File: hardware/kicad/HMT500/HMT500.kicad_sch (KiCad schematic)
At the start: 0 parts

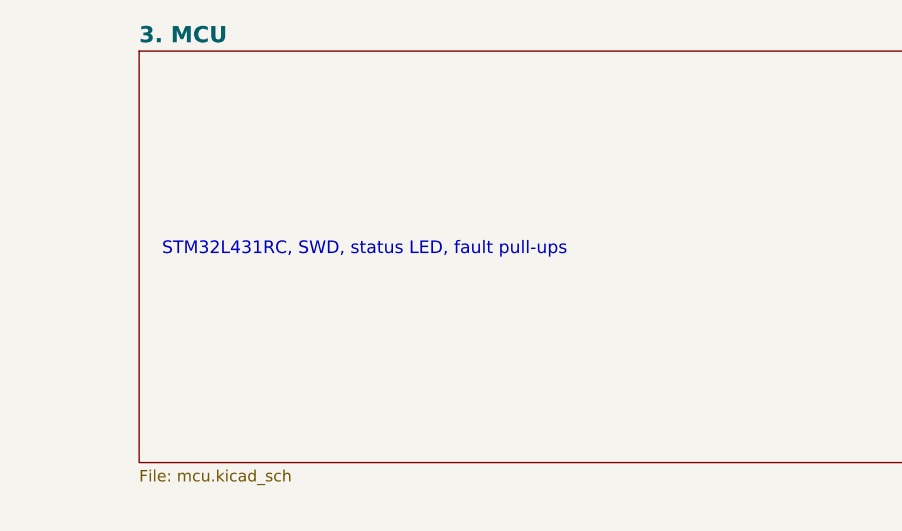
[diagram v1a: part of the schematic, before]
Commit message: Switch MCU to STM32G0B1CCT3 (in-house part, 125 C grade)
DOTECH already uses the STM32G0B1CCT6 in DP2000. Use the -40..125 C
grade of the same chip so tooling, drivers and production fixtures
can be shared.

- Schematic: new LQFP48 symbol with pin numbers from the official
  KiCad STM32G0B1C_B-C-E_Tx symbol. NRST is on PF2. BOOT0 shares
  PA14/SWCLK, so the pull-down is removed and the option bytes select
  flash boot. SWO is gone (Cortex-M0+), so J2 pin 6 is NC. VREF+ is
  fed from the FB2 filter. Faults and alarms move to PB13-15. The
  netlist check passes: 69 nets, 0 errors.
- Pin table, block design, BOM and cost updated. The bootloader doc
  now covers G0B1 dual-bank page erase, the prefetch erratum and the
  option bytes.
- Mech: MCU footprint in the 3D and drawings is now 7x7. STEP files,
  renders and the KiCad board regenerated.
- MCU review: fix product names read from the purchase report
  (HPX3000, HTP1100W) and mark the decision.

Co-Authored-By: Claude Opus 5.5 <noreply@anthropic.com>
Claude-Session: https://claude.ai/code/session_01JA2o8uJsqp9Vzsg4b665ev
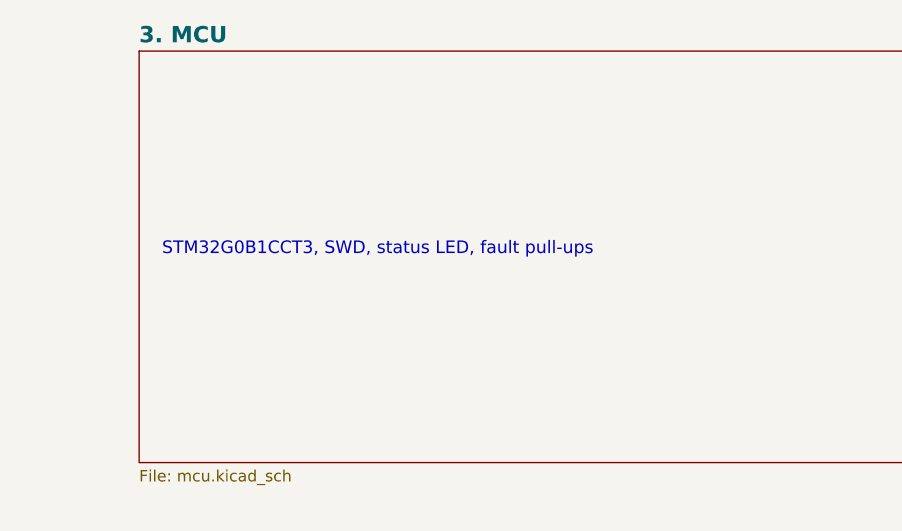
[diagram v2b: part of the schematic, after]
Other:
- note added: "STM32G0B1CCT3, SWD, status LED, fault pull-ups"
- note removed: "STM32L431RC, SWD, status LED, fault pull-ups"
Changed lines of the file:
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@@
 (text "eFuse (reverse/OV/UV), 60V buck to 5V, LDO 3.3V" (at 160.02 78.74 0) (effects (font (size 1.4 1.4)) (justify left bottom)))
 (sheet (at 284.48 55.88) (size 106.68 45.72) (fields_autoplaced) (stroke (width 0.1524) (type solid)) (fill (color 0 0 0 0.0000)) (property "Sheetname" "3. MCU" (at 284.48 55.118 0) (effects (font (size 1.8 1.8) bold) (justify left bottom))) (property "Sheetfile" "mcu.kicad_sch" (at 284.48 102.362 0) (effects (font (size 1.27 1.27)) (justify left top))) (instances (project "HMT500" (path "/1ebb025b-11bd-5f7c-aaab-41e2a750e8b3" (page "4")))))
-(text "STM32L431RC, SWD, status LED, fault pull-ups" (at 287.02 78.74 0) (effects (font (size 1.4 1.4)) (justify left bottom)))
+(text "STM32G0B1CCT3, SWD, status LED, fault pull-ups" (at 287.02 78.74 0) (effects (font (size 1.4 1.4)) (justify left bottom)))
 (sheet (at 30.48 132.08) (size 106.68 45.72) (fields_autoplaced) (stroke (width 0.1524) (type solid)) (fill (color 0 0 0 0.0000)) (property "Sheetname" "4. Measurement" (at 30.48 131.318 0) (effects (font (size 1.8 1.8) bold) (justify left bottom))) (property "Sheetfile" "measurement.kicad_sch" (at 30.48 178.562 0) (effects (font (size 1.27 1.27)) (justify left top))) (instances (project "HMT500" (path "/1ebb025b-11bd-5f7c-aaab-41e2a750e8b3" (page "5")))))
 (text "Capacitive humidity sensor (PCAP04) and Pt1000 4-wire (ADS1220)" (at 33.02 154.94 0) (effects (font (size 1.4 1.4)) (justify left bottom)))

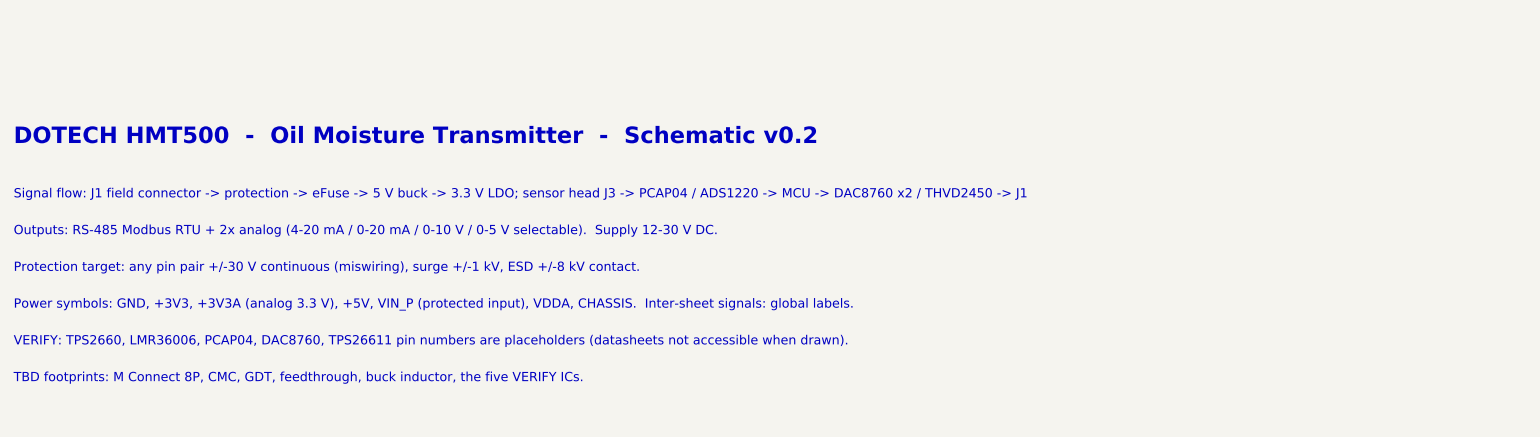
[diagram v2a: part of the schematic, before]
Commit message: Schematic v0.3, purchase parts list, studio product renders
- Schematic v0.3: TPS26600PWPR now uses the official KiCad pinout
  (HTSSOP-16: dual IN/OUT, UVLO, OVP, SHDN, MODE, RTN, EP). RTN is
  split onto its own net EF_RTN with a 0R link R22, flagged for
  datasheet confirmation, because tying RTN to GND disables the
  reverse-polarity protection. The ADS1220 pinout matches the official
  symbol. Netlist check passes: 70 nets, 0 errors. Rev bumped and cover
  notes updated.
- make_parts_list.py: purchase parts list (xlsx + csv) built from the
  KiCad BOM. It adds manufacturer, MPN, 1k price estimates and status,
  plus a per-category summary sheet with an FX input.
- render_studio.py: studio-style product renders (PBR stainless,
  image-based lighting, SSAO, contact shadow, laser marking, thread and
  connector pin detail). Six shots, including a cutaway.

Co-Authored-By: Claude Opus 5.5 <noreply@anthropic.com>
Claude-Session: https://claude.ai/code/session_01JA2o8uJsqp9Vzsg4b665ev
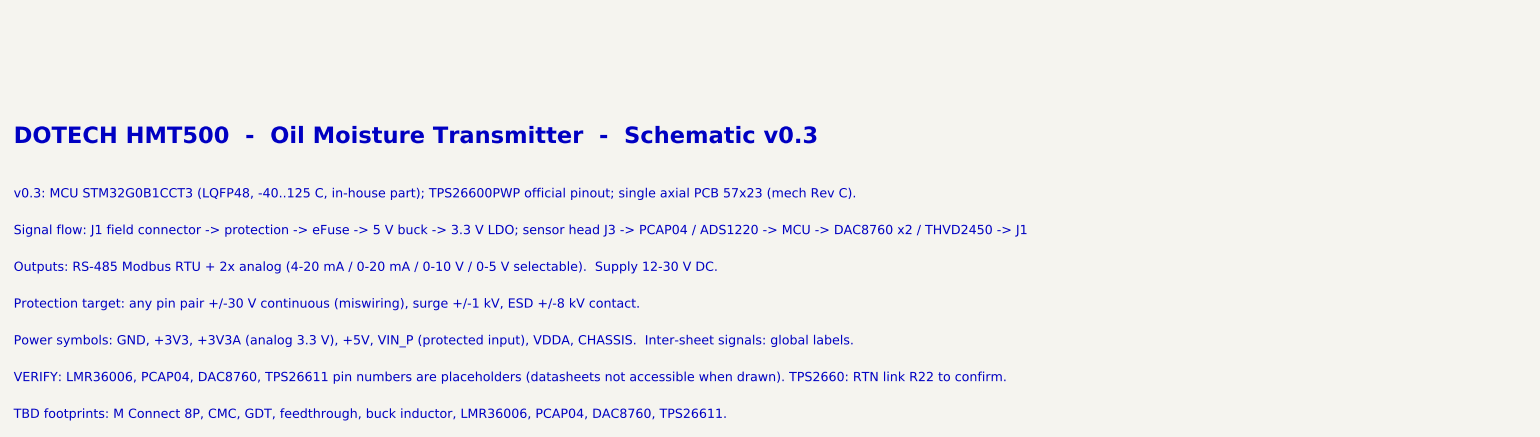
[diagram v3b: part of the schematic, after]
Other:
- note added: "DOTECH HMT500 - Oil Moisture Transmitter - Schematic v0.3"
- note added: "TBD footprints: M Connect 8P, CMC, GDT, feedthrough, buck inductor, LMR36006, PCAP04, DAC8760, TPS26611."
- note added: "VERIFY: LMR36006, PCAP04, DAC8760, TPS26611 pin numbers are placeholders (datasheets not accessible when drawn). TPS2660: RTN link R22 to confirm."
- note added: "v0.3: MCU STM32G0B1CCT3 (LQFP48, -40..125 C, in-house part); TPS26600PWP official pinout; single axial PCB 57x23 (mech Rev C)."
- note removed: "DOTECH HMT500 - Oil Moisture Transmitter - Schematic v0.2"
- note removed: "TBD footprints: M Connect 8P, CMC, GDT, feedthrough, buck inductor, the five VERIFY ICs."
- note removed: "VERIFY: TPS2660, LMR36006, PCAP04, DAC8760, TPS26611 pin numbers are placeholders (datasheets not accessible when drawn)."
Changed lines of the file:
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@@
 (kicad_sch (version 20230121) (generator eeschema) (paper "A3")
-(title_block (title "HMT500  Top") (date "2026-09-26") (rev "0.2") (company "DOTECH Co., Ltd.") (comment 1 "Oil moisture transmitter HMT500 - RS-485 + 2x V/I analog output") (comment 2 "Design notes: docs/hw/circuit-design.md") (comment 3 "VERIFY=YES parts: placeholder pin numbers (TPS2660, LMR36006, PCAP04, DAC8760, TPS26611)"))
+(title_block (title "HMT500  Top") (date "2026-09-26") (rev "0.3") (company "DOTECH Co., Ltd.") (comment 1 "Oil moisture transmitter HMT500 - RS-485 + 2x V/I analog output") (comment 2 "Design notes: docs/hw/circuit-design.md") (comment 3 "VERIFY=YES parts: placeholder pin numbers (LMR36006, PCAP04, DAC8760, TPS26611); TPS2660 RTN wiring"))
 (sheet (at 30.48 55.88) (size 106.68 45.72) (fields_autoplaced) (stroke (width 0.1524) (type solid)) (fill (color 0 0 0 0.0000)) (property "Sheetname" "1. Connector & input protection" (at 30.48 55.118 0) (effects (font (size 1.8 1.8) bold) (justify left bottom))) (property "Sheetfile" "connector.kicad_sch" (at 30.48 102.362 0) (effects (font (size 1.27 1.27)) (justify left top))) (instances (project "HMT500" (path "/1ebb025b-11bd-5f7c-aaab-41e2a750e8b3" (page "2")))))
 (text "Field connector, 2-stage bidirectional TVS surge protection, chassis isolation" (at 33.02 78.74 0) (effects (font (size 1.4 1.4)) (justify left bottom)))
@@
 (sheet (at 284.48 132.08) (size 106.68 45.72) (fields_autoplaced) (stroke (width 0.1524) (type solid)) (fill (color 0 0 0 0.0000)) (property "Sheetname" "6. RS-485" (at 284.48 131.318 0) (effects (font (size 1.8 1.8) bold) (justify left bottom))) (property "Sheetfile" "rs485.kicad_sch" (at 284.48 178.562 0) (effects (font (size 1.27 1.27)) (justify left top))) (instances (project "HMT500" (path "/1ebb025b-11bd-5f7c-aaab-41e2a750e8b3" (page "7")))))
 (text "THVD2450 +/-70V fault-protected transceiver" (at 287.02 154.94 0) (effects (font (size 1.4 1.4)) (justify left bottom)))
-(text "DOTECH HMT500  -  Oil Moisture Transmitter  -  Schematic v0.2" (at 30.48 223.52 0) (effects (font (size 2.5 2.5) bold) (justify left bottom)))
-(text "Signal flow: J1 field connector -> protection -> eFuse -> 5 V buck -> 3.3 V LDO; sensor head J3 -> PCAP04 / ADS1220 -> MCU -> DAC8760 x2 / THVD2450 -> J1" (at 30.48 231.648 0) (effects (font (size 1.4 1.4)) (justify left bottom)))
-(text "Outputs: RS-485 Modbus RTU + 2x analog (4-20 mA / 0-20 mA / 0-10 V / 0-5 V selectable).  Supply 12-30 V DC." (at 30.48 237.236 0) (effects (font (size 1.4 1.4)) (justify left bottom)))
-(text "Protection target: any pin pair +/-30 V continuous (miswiring), surge +/-1 kV, ESD +/-8 kV contact." (at 30.48 242.824 0) (effects (font (size 1.4 1.4)) (justify left bottom)))
-(text "Power symbols: GND, +3V3, +3V3A (analog 3.3 V), +5V, VIN_P (protected input), VDDA, CHASSIS.  Inter-sheet signals: global labels." (at 30.48 248.412 0) (effects (font (size 1.4 1.4)) (justify left bottom)))
-(text "VERIFY: TPS2660, LMR36006, PCAP04, DAC8760, TPS26611 pin numbers are placeholders (datasheets not accessible when drawn)." (at 30.48 254 0) (effects (font (size 1.4 1.4)) (justify left bottom)))
-(text "TBD footprints: M Connect 8P, CMC, GDT, feedthrough, buck inductor, the five VERIFY ICs." (at 30.48 259.588 0) (effects (font (size 1.4 1.4)) (justify left bottom)))
+(text "DOTECH HMT500  -  Oil Moisture Transmitter  -  Schematic v0.3" (at 30.48 223.52 0) (effects (font (size 2.5 2.5) bold) (justify left bottom)))
+(text "v0.3: MCU STM32G0B1CCT3 (LQFP48, -40..125 C, in-house part); TPS26600PWP official pinout; single axial PCB 57x23 (mech Rev C)." (at 30.48 231.648 0) (effects (font (size 1.4 1.4)) (justify left bottom)))
+(text "Signal flow: J1 field connector -> protection -> eFuse -> 5 V buck -> 3.3 V LDO; sensor head J3 -> PCAP04 / ADS1220 -> MCU -> DAC8760 x2 / THVD2450 -> J1" (at 30.48 237.236 0) (effects (font (size 1.4 1.4)) (justify left bottom)))
+(text "Outputs: RS-485 Modbus RTU + 2x analog (4-20 mA / 0-20 mA / 0-10 V / 0-5 V selectable).  Supply 12-30 V DC." (at 30.48 242.824 0) (effects (font (size 1.4 1.4)) (justify left bottom)))
+(text "Protection target: any pin pair +/-30 V continuous (miswiring), surge +/-1 kV, ESD +/-8 kV contact." (at 30.48 248.412 0) (effects (font (size 1.4 1.4)) (justify left bottom)))
+(text "Power symbols: GND, +3V3, +3V3A (analog 3.3 V), +5V, VIN_P (protected input), VDDA, CHASSIS.  Inter-sheet signals: global labels." (at 30.48 254 0) (effects (font (size 1.4 1.4)) (justify left bottom)))
+(text "VERIFY: LMR36006, PCAP04, DAC8760, TPS26611 pin numbers are placeholders (datasheets not accessible when drawn). TPS2660: RTN link R22 to confirm." (at 30.48 259.588 0) (effects (font (size 1.4 1.4)) (justify left bottom)))
+(text "TBD footprints: M Connect 8P, CMC, GDT, feedthrough, buck inductor, LMR36006, PCAP04, DAC8760, TPS26611." (at 30.48 265.176 0) (effects (font (size 1.4 1.4)) (justify left bottom)))
 (sheet_instances (path "/" (page "1")))
 )
